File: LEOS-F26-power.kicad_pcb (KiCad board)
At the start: 2 copper layers, 100 x 100 mm, 18 parts, among them J1 MicroFit_1x4, J2 MicroFit_1x4, U1 MCP2518FD, U2 MCP2562FD, Y1 40 MHz

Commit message: updates to BOM
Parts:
- added C-1: 4.7uF, Capacitor_SMD:C_0805_2012Metric, F.Cu at (128.0, 94.4)
- added C-10: 0.1u, Capacitor_SMD:C_0805_2012Metric, F.Cu at (128.0, 115.5)
- added C-2: 4.7uF, Capacitor_SMD:C_0805_2012Metric, F.Cu at (128.0, 97.4)
- added C-3: 4.7uF, Capacitor_SMD:C_0805_2012Metric, F.Cu at (128.0, 100.5)
- added C-4: 4.7uF, Capacitor_SMD:C_0805_2012Metric, F.Cu at (128.0, 103.5)
- added C-5: 0.1u, Capacitor_SMD:C_0805_2012Metric, F.Cu at (128.0, 106.5)
- added C-6: 620p, Capacitor_SMD:C_0805_2012Metric, F.Cu at (128.0, 109.5)
- added C-7: 6.8p, Capacitor_SMD:C_0805_2012Metric, F.Cu at (128.0, 112.5)
- added C-8: 47u, LEOS:CAPAE660X600N, F.Cu at (133.2, 115.0)
- added C-9: 47u, Capacitor_SMD:C_1206_3216Metric, F.Cu at (133.2, 118.4)
- added C_1: 4.7uF, Capacitor_SMD:C_0805_2012Metric, F.Cu at (158.1, 121.0)
- added C_2: 4.7uF, Capacitor_SMD:C_0805_2012Metric, F.Cu at (158.1, 124.0)
- added C_3: 4.7uF, Capacitor_SMD:C_0805_2012Metric, F.Cu at (158.1, 127.0)
- added C_4: 4.7uF, Capacitor_SMD:C_0805_2012Metric, F.Cu at (158.1, 130.0)
- added C_5: 0.1u, Capacitor_SMD:C_0805_2012Metric, F.Cu at (158.1, 133.1)
- added C_6: 4.7n, Capacitor_SMD:C_0805_2012Metric, F.Cu at (158.1, 136.1)
- added C_7: 6.8p, Capacitor_SMD:C_0805_2012Metric, F.Cu at (158.1, 139.1)
- added C_8: 47u, LEOS:CAPAE660X600N, F.Cu at (167.6, 136.4)
- added C_9: 47u, Capacitor_SMD:C_1206_3216Metric, F.Cu at (167.6, 139.8)
- added CdVdt1: 4.7n, Capacitor_SMD:C_0805_2012Metric, F.Cu at (176.5, 94.0)
- added Cin1: 0.1u, Capacitor_SMD:C_0805_2012Metric, F.Cu at (178.0, 104.1)
- added Cin2: 10uF, Capacitor_SMD:C_0805_2012Metric, F.Cu at (180.5, 104.0)
- added Cout1: 10uF, Capacitor_SMD:C_0805_2012Metric, F.Cu at (166.5, 103.5)
- added Cout2: 10uF, Capacitor_SMD:C_0805_2012Metric, F.Cu at (164.0, 103.5)
- added D-1: 60V 20A, Diode_THT:D_DO-201AD_P15.24mm_Horizontal, F.Cu at (133.9, 122.5)
- added D_1: 60V 20A, Diode_THT:D_DO-201AD_P15.24mm_Horizontal, F.Cu at (172.6, 136.2)
- added J3: Power Input, Connector_AMASS:AMASS_XT60IPW-M_1x03_P7.20mm_Horizontal, F.Cu at (183.0, 88.2)
- added J4: 5V, Connector_JST:JST_XH_S2B-XH-A_1x02_P2.50mm_Horizontal, F.Cu at (190.1, 111.2)
- added J5: 5V, Connector_JST:JST_XH_S2B-XH-A_1x02_P2.50mm_Horizontal, F.Cu at (190.0, 120.0)
- added J6: 5V, Connector_JST:JST_XH_S2B-XH-A_1x02_P2.50mm_Horizontal, F.Cu at (190.1, 128.8)
- added J7: 1-18V, Connector_JST:JST_XH_S2B-XH-A_1x02_P2.50mm_Horizontal, F.Cu at (109.9, 108.2)
- added J8: 1-18V, Connector_JST:JST_XH_S2B-XH-A_1x02_P2.50mm_Horizontal, F.Cu at (109.9, 117.2)
- added J9: 1-18V, Connector_JST:JST_XH_S2B-XH-A_1x02_P2.50mm_Horizontal, F.Cu at (109.9, 126.2)
- added L-1: 10uH, LEOS:IND_BOURNS_SRR1280, F.Cu at (138.3, 107.5)
- added L_1: 4.7uH, LEOS:IND_SRP7028A-4R7M_BRN, F.Cu at (170.3, 123.8)
- added R-1: 365k, Resistor_SMD:R_0805_2012Metric, F.Cu at (132.4, 94.4)
- added R-2: 88.7, Resistor_SMD:R_0805_2012Metric, F.Cu at (132.4, 97.3)
- added R-3: 390k, Resistor_SMD:R_0805_2012Metric, F.Cu at (132.4, 100.3)
- added R-4: 56.2k, Resistor_SMD:R_0805_2012Metric, F.Cu at (132.4, 103.2)
- added R-5: 1.1k, Resistor_SMD:R_0805_2012Metric, F.Cu at (132.4, 106.2)
- added R-6: 25.5k, Resistor_SMD:R_0805_2012Metric, F.Cu at (132.4, 109.2)
- added R.1: 150k, Resistor_THT:R_Axial_DIN0207_L6.3mm_D2.5mm_P10.16mm_Horizontal, F.Cu at (150.9, 82.5)
- added R.2: 10k, Resistor_THT:R_Axial_DIN0207_L6.3mm_D2.5mm_P10.16mm_Horizontal, F.Cu at (150.9, 86.5)
- added R_1: 365k, Resistor_SMD:R_0805_2012Metric, F.Cu at (162.5, 121.0)
- added R_2: 88.7, Resistor_SMD:R_0805_2012Metric, F.Cu at (162.5, 123.9)
- added R_3: 147k, Resistor_SMD:R_0805_2012Metric, F.Cu at (162.5, 126.9)
- added R_4: 23.7k, Resistor_SMD:R_0805_2012Metric, F.Cu at (162.5, 129.8)
- added R_5: 60.4k, Resistor_SMD:R_0805_2012Metric, F.Cu at (162.5, 132.8)
- added R_6: 11.5k, Resistor_SMD:R_0805_2012Metric, F.Cu at (162.5, 135.7)
- added R_ILIM1: 3.0k, Resistor_SMD:R_0805_2012Metric, F.Cu at (166.5, 96.0)
- added TP1-18: TestPoint, TestPoint:TestPoint_Loop_D2.60mm_Drill0.9mm_Beaded, F.Cu at (109.5, 101.5)
- added TPFB1-18: TestPoint, TestPoint:TestPoint_Loop_D2.60mm_Drill0.9mm_Beaded, F.Cu at (158.9, 98.2)
- added TPFB5: TestPoint, TestPoint:TestPoint_Loop_D2.60mm_Drill0.9mm_Beaded, F.Cu at (151.9, 98.2)
- added TPGND2: GND TestPoint, TestPoint:TestPoint_Loop_D2.60mm_Drill0.9mm_Beaded, F.Cu at (103.5, 101.0)
- added TPUVLO1: TestPoint, TestPoint:TestPoint_Loop_D2.60mm_Drill0.9mm_Beaded, F.Cu at (151.9, 91.1)
- added U3: TPS54540BDDA, LEOS:SO-POWERPAD8_DDA_TEX, F.Cu at (169.0, 131.4)
- added U4: TPS16630PWPR, LEOS:HTSSOP20_PWP_TEX, F.Cu at (172.0, 100.1)
- added U5: TPS54540BDDA, LEOS:SO-POWERPAD8_DDA_TEX, F.Cu at (122.7, 125.6)
- added U6: MCP41HV51-104E/MQ, LEOS:QFN20_5x5MC_MCH, F.Cu at (139.8, 93.9)
- renumbered TP3 to TP5V1, TP4 to TPGND1
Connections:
- A1 pad 14: unconnected-(A1-GPIO10-Pad14) -> /SCK1
- A1 pad 15: unconnected-(A1-GPIO11-Pad15)_1 -> /MOSI1
- A1 pad 16: unconnected-(A1-GPIO12-Pad16) -> /MISO1
- A1 pad 17: unconnected-(A1-GPIO13-Pad17) -> /CS1
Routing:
- added copper zone on F.Cu, net +BATT
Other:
- board text removed: "Be sure to update the information block at the bottom of the page! (Then delete me)"

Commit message: efuse routing
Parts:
- moved R.1 24.0 mm to (172.0, 94.0), turned to 180 degrees
- moved Cin2 12.6 mm to (174.5, 93.0), turned to 90 degrees
- moved R.2 11.8 mm to (161.8, 91.0)
- moved Cin1 11.1 mm to (177.0, 93.0), turned to 90 degrees
- moved Cout2 10.8 mm to (174.5, 106.0)
- moved Cout1 10.3 mm to (176.5, 106.0)
- moved CdVdt1 10.3 mm to (167.0, 98.0), turned to -90 degrees
- moved R_ILIM1 6.47 mm to (167.0, 102.4)
- turned U4 to -90 degrees
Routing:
- net Net-(U4-UVLO): track 0.00 -> 14.0 mm
- net +BATT: track 0.00 -> 3.49 mm
- net Net-(U4-ILIM): track 0.00 -> 2.22 mm
- net Net-(U4-DVDT): track 0.00 -> 2.19 mm
- net GND: vias 22 -> 42
- added copper zone on In1.Cu, net GND
- added copper zone on F.Cu, net VPP
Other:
- copper layers 2 -> 4

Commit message: efuse routing 2
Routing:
- net GND: track 4.46 -> 15.2 mm, vias 42 -> 40
- net +BATT: track 3.49 -> 6.02 mm
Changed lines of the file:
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@@
+	)
+	(segment
+		(start 169.772299 97.172313)
+		(end 170.422285 97.172313)
+		(width 0.25)
+		(layer "F.Cu")
+		(net "GND")
+	)
+	(segment
+		(start 169.772299 98.772299)
+		(end 170 99)
+		(width 0.25)
+		(layer "F.Cu")
+		(net "GND")
+	)
+	(segment
+		(start 167 98.9)
+		(end 168.9 98.9)
+		(width 1)
+		(layer "F.Cu")
+		(net "GND")
 	)
 	(segment
@@
 	)
 	(segment
+		(start 174.5 106.95)
+		(end 176.5 106.95)
+		(width 0.5)
+		(layer "F.Cu")
+		(net "GND")
+	)
+	(segment
+		(start 167 98.9)
+		(end 167 101.5)
+		(width 1)
+		(layer "F.Cu")
+		(net "GND")
+	)
+	(segment
+		(start 168.9 98.9)
+		(end 169 99)
+		(width 1)
+		(layer "F.Cu")
+		(net "GND")
+	)
+	(segment
 		(start 124.512501 73.512501)
 		(end 124.45 73.575001)
@@
 	)
 	(segment
+		(start 169.772299 97.172313)
+		(end 169.772299 98.772299)
+		(width 0.25)
+		(layer "F.Cu")
+		(net "GND")
+	)
+	(segment
+		(start 176.5 106.95)
+		(end 177.95 106.95)
+		(width 0.5)
+		(layer "F.Cu")
+		(net "GND")
+	)
+	(segment
+		(start 177.95 106.95)
+		(end 178 107)
+		(width 0.5)
+		(layer "F.Cu")
+		(net "GND")
+	)
+	(segment
 		(start 125.025001 73)
 		(end 124.512501 73.512501)
@@
 	)
 	(via
-		(at 179 107)
-		(size 0.6)
-		(drill 0.3)
-		(layers "F.Cu" "B.Cu")
-		(free yes)
-		(net "GND")
-	)
-	(via
 		(at 136.25 78)
 		(size 0.6)
@@
 		)
 		(filling no)
-		(net "GND")
-	)
-	(via
-		(at 168 100)
-		(size 0.6)
-		(drill 0.3)
-		(layers "F.Cu" "B.Cu")
-		(free yes)
 		(net "GND")
 	)
@@
 	)
 	(segment
+		(start 174.45 94)
+		(end 174.5 93.95)
+		(width 1)
+		(layer "F.Cu")
+		(net "+BATT")
+	)
+	(segment
 		(start 171.722257 97.172313)
 		(end 171.722257 96.277743)
@@
 		(end 174 95.5)
 		(width 0.2)
+		(layer "F.Cu")
+		(net "+BATT")
+	)
+	(segment
+		(start 172 94)
+		(end 174.45 94)
+		(width 1)
 		(layer "F.Cu")
 		(net "+BATT")
@@
 	)
 	(zone
-		(net "GND")
-		(layer "F.Cu")
-		(name "GND_5")
-		(hatch edge 0.5)
-		(priority 12)
-		(connect_pads
-			(clearance 0.25)
-		)
-		(min_thickness 0.25)
-		(fill
-			(thermal_gap 0.3)
-			(thermal_bridge_width 0.5)
-			(island_removal_mode 0)
-		)
-		(polygon
-			(pts
-				(xy 173.5 106) (xy 180 106) (xy 180 108) (xy 173.5 108)
-			)
-		)
-	)
-	(zone
 		(net "+BATT")
 		(layer "F.Cu")
@@
 		(polygon
 			(pts
-				(xy 170 89) (xy 178 89) (xy 178 93) (xy 170 93)
+				(xy 170 89) (xy 179 89) (xy 179 93) (xy 170 93)
 			)
 		)
@@
 				(xy 131.116421 72.282843) (xy 131.257842 72.141422) (xy 130.931066 71.743934) (xy 130.675706 71.700707)
 				(xy 130.846465 72.29573)
-			)
-		)
-	)
-	(zone
-		(net "+BATT")
-		(layer "F.Cu")
-		(name "BATT_2")
-		(hatch edge 0.5)
-		(priority 5)
-		(connect_pads
-			(clearance 0.25)
-		)
-		(min_thickness 0.25)
-		(fill yes
-			(thermal_gap 0.3)
-			(thermal_bridge_width 0.5)
-			(island_removal_mode 0)
-		)
-		(polygon
-			(pts
-				(xy 173.5 93) (xy 171 93) (xy 171 95) (xy 173.5 95)
 			)
 		)
@@
 		(polygon
 			(pts
-				(xy 166 98) (xy 174 98) (xy 174 102) (xy 166 102)
+				(xy 168 98) (xy 174 98) (xy 174 102) (xy 168 102)
 			)
 		)
@@
 		(net "GND")
 		(layer "F.Cu")
-		(name "GND_2")
 		(hatch edge 0.5)
-		(priority 9)
+		(priority 2)
+		(connect_pads
+			(clearance 0.25)
+		)
+		(min_thickness 0.25)
+		(fill yes
+			(thermal_gap 0.25)
+			(thermal_bridge_width 0.5)
+			(island_removal_mode 0)
+		)
+		(polygon
+			(pts
+				(xy 109 74.5) (xy 109 78) (xy 113.5 78) (xy 113.5 74.5)
+			)
+		)
+	)
+	(zone
+		(net "+BATT")
+		(layer "F.Cu")
+		(name "BATT_1")
+		(hatch edge 0.5)
+		(priority 4)
 		(connect_pads
 			(clearance 0.25)
@@
 		(polygon
 			(pts
-				(xy 169.5 96.3) (xy 170.7 96.3) (xy 170.7 98.1) (xy 169.5 98.1)
+				(xy 173.5 98) (xy 173.5 93) (xy 178.5 93) (xy 178.5 98)
 			)
 		)
-	)
-	(zone
-		(net "GND")
-		(layer "F.Cu")
-		(hatch edge 0.5)
-		(priority 2)
-		(connect_pads
-			(clearance 0.25)
-		)
-		(min_thickness 0.25)
-		(fill yes
-			(thermal_gap 0.25)
-			(thermal_bridge_width 0.5)
-			(island_removal_mode 0)
-		)
-		(polygon
-			(pts
-				(xy 109 74.5) (xy 109 78) (xy 113.5 78) (xy 113.5 74.5)
-			)
-		)
-	)
-	(zone
-		(net "+BATT")
-		(layer "F.Cu")
-		(name "BATT_1")
-		(hatch edge 0.5)
-		(priority 4)
-		(connect_pads
-			(clearance 0.25)
-		)
-		(min_thickness 0.25)
-		(fill yes
-			(thermal_gap 0.3)
-			(thermal_bridge_width 0.5)
-			(island_removal_mode 0)
-		)
-		(polygon
-			(pts
-				(xy 173.5 98) (xy 173.5 93) (xy 175.5 93) (xy 175.5 98)
-			)
-		)

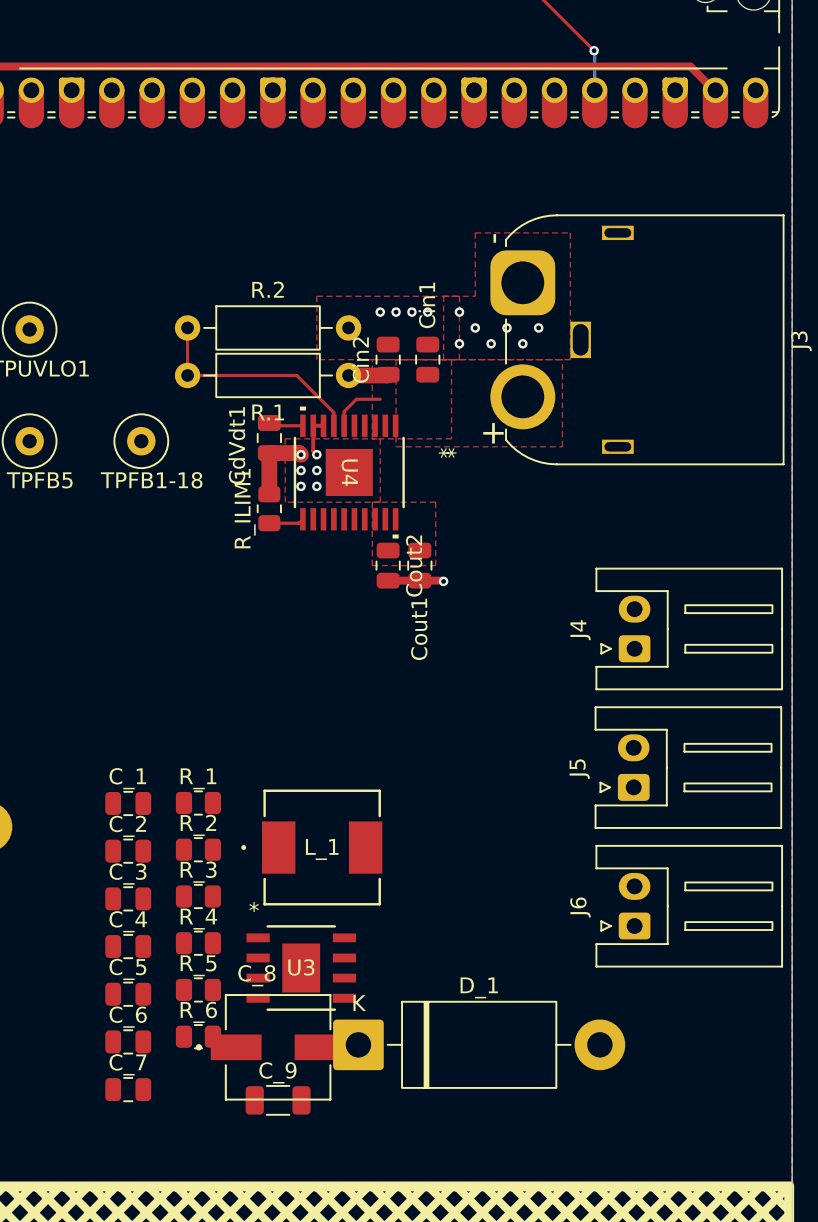
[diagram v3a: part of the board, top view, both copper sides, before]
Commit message: buck converter routing
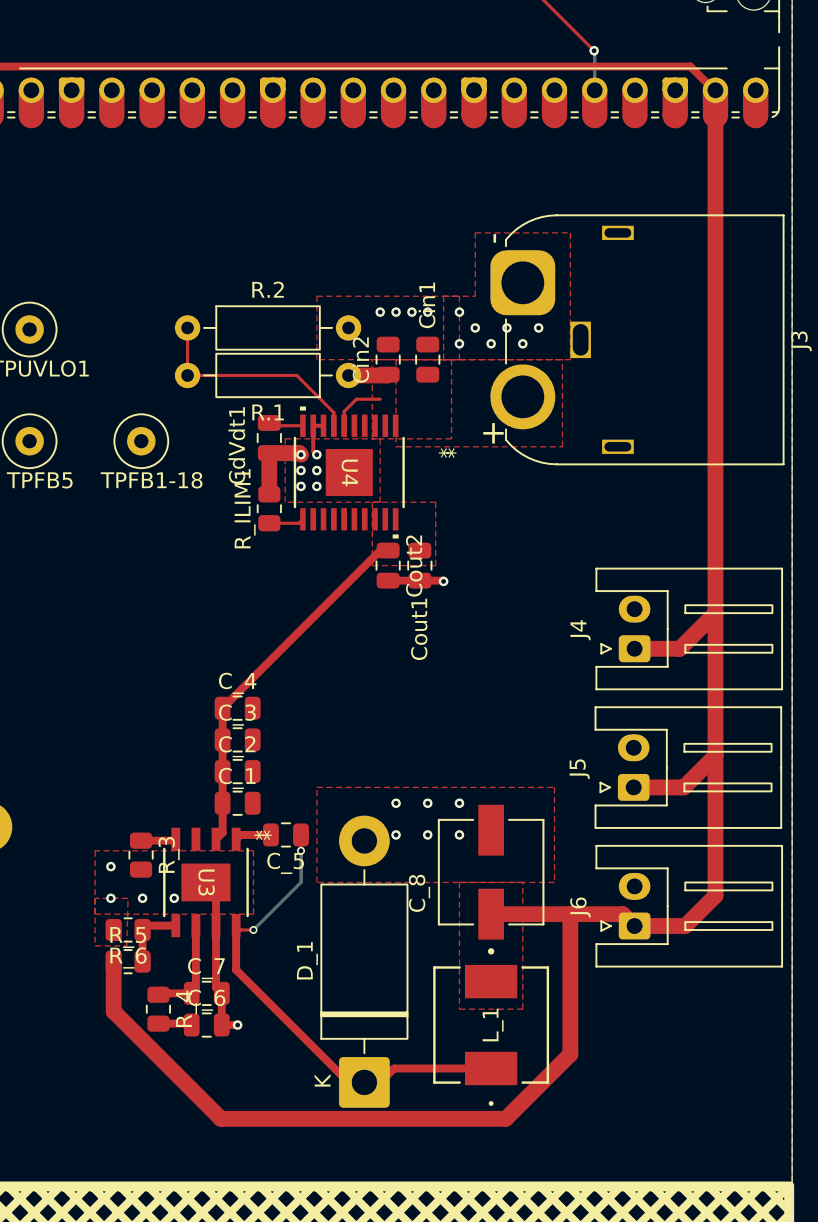
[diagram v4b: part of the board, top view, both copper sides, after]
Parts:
- removed C_9: 47u, Capacitor_SMD:C_1206_3216Metric
- removed R_1: 365k, Resistor_SMD:R_0805_2012Metric
- removed R_2: 88.7, Resistor_SMD:R_0805_2012Metric
- moved C_8 17.4 mm to (181.0, 125.3), turned to 90 degrees
- moved C_4 16.6 mm to (165.0, 115.0)
- moved L_1 15.5 mm to (181.0, 135.0), turned to 90 degrees
- moved C_5 14.1 mm to (168.1, 123.0), turned to 180 degrees
- moved C_3 12.2 mm to (165.0, 117.0)
- moved C_2 8.54 mm to (165.0, 119.0)
- moved U3 8.08 mm to (163.0, 126.0), turned to -90 degrees
- moved R_6 8.07 mm to (158.1, 129.0), turned to 180 degrees
- moved C_7 7.84 mm to (163.1, 133.0)
- moved C_1 6.91 mm to (165.0, 121.0)
- moved C_6 5.07 mm to (163.1, 135.0)
- moved R_4 4.87 mm to (160.0, 134.0), turned to -90 degrees
- moved R_5 4.78 mm to (158.1, 131.0)
- moved R_3 4.46 mm to (158.9, 124.3), turned to -90 degrees
- moved D_1 2.40 mm to (173.0, 138.6), turned to 90 degrees
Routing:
- net +5V: track 104.0 -> 226.7 mm
- net Net-(D_1-K): track 0.00 -> 29.7 mm, vias 0 -> 2
- net VPP: track 0.00 -> 23.0 mm
- net GND: track 15.2 -> 25.6 mm, vias 40 -> 51
- net Net-(U3-COMP): track 0.00 -> 6.52 mm
- net /5V Power/FB: track 0.00 -> 4.21 mm
- net Net-(U3-BOOT): track 0.00 -> 2.31 mm
- net Net-(U3-RT/CLK): track 0.00 -> 2.23 mm
- net Net-(C_6-Pad1): track 0.00 -> 2.14 mm

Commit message: routing done
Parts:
- removed C-9: 47u, Capacitor_SMD:C_1206_3216Metric
- removed R-1: 365k, Resistor_SMD:R_0805_2012Metric
- removed R-2: 88.7, Resistor_SMD:R_0805_2012Metric
- moved C-10 25.2 mm to (126.5, 90.3)
- moved C-8 21.1 mm to (126.5, 135.0), turned to -90 degrees
- moved L-1 19.5 mm to (126.0, 122.6), turned to -90 degrees
- moved U5 19.3 mm to (127.5, 106.8), turned to 180 degrees
- moved D-1 15.9 mm to (119.4, 116.0)
- moved C-1 14.2 mm to (134.0, 107.3), turned to -90 degrees
- moved R-4 13.5 mm to (119.0, 104.8), turned to 180 degrees
- moved C-2 12.7 mm to (136.0, 107.3), turned to -90 degrees
- moved C-4 12.6 mm to (140.0, 107.3), turned to -90 degrees
- moved C-3 12.1 mm to (138.0, 107.3), turned to -90 degrees
- moved R-6 11.2 mm to (123.5, 102.3)
- moved R-5 10.7 mm to (123.5, 100.3), turned to 180 degrees
- moved C-6 10.1 mm to (118.0, 107.8), turned to -90 degrees
- moved C-7 9.22 mm to (120.0, 107.9), turned to -90 degrees
- moved U6 7.01 mm to (132.8, 94.3), turned to 180 degrees
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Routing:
- net VPP: track 23.0 -> 28.8 mm
- net Net-(U5-COMP): track 0.00 -> 2.14 mm
- net Net-(C-6-Pad1): track 0.00 -> 2.09 mm
- net /1-18V Power/FB1: track 0.00 -> 2.00 mm
- net Net-(D_1-K): vias 2 -> 0

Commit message: updates to BOM
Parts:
- moved TPFB5 37.5 mm to (152.1, 135.6)
- moved TPFB1-18 33.1 mm to (125.9, 95.3)
- moved TPGND2 16.3 mm to (118.9, 95.7)
- moved C-9 13.2 mm to (139.5, 88.0)
- moved TPUVLO1 11.6 mm to (162.0, 85.5)
- moved C-8 10.5 mm to (134.5, 128.2), turned to 90 degrees
- moved U6 5.96 mm to (138.6, 92.8)
- moved R-1 5.07 mm to (129.0, 102.5), turned to 180 degrees
- moved TP1-18 4.61 mm to (105.0, 100.5)
- moved L-1 4.61 mm to (123.0, 126.1)
- moved R-3 2.00 mm to (124.5, 102.1), turned to 90 degrees
- moved C-7 1.44 mm to (120.5, 106.5)
- moved C-6 1.44 mm to (118.5, 106.5)
- moved R-2 1.44 mm to (119.5, 103.5)
- moved C-1 1.30 mm to (134.5, 108.5)
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- renumbered C-10 to C-9, R-3 to R-1, R-4 to R-2, R-5 to R-3, R-6 to R-4, R_3 to R_1, R_4 to R_2, R_5 to R_3, R_6 to R_4
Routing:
- net VDC: track 0.00 -> 89.4 mm
- net GND: track 25.6 -> 78.1 mm, vias 51 -> 72
- net VDD: track 90.8 -> 141.7 mm, vias 3 -> 7
- net /CS1: track 0.00 -> 48.9 mm, vias 0 -> 2
- net /SCK1: track 0.00 -> 48.8 mm, vias 0 -> 2
- net /MOSI1: track 0.00 -> 47.7 mm, vias 0 -> 2
- net /MISO1: track 0.00 -> 44.9 mm, vias 0 -> 2
- net VPP: track 28.8 -> 63.0 mm
- net Net-(D-1-K): track 0.00 -> 25.3 mm
- net /1-18V Power/POT: track 0.00 -> 15.8 mm
- net /1-18V Power/FB1: track 2.00 -> 12.9 mm, vias 0 -> 2
- net /5V Power/FB: track 4.21 -> 13.7 mm, vias 0 -> 2
- net Net-(U4-UVLO): track 14.0 -> 19.6 mm
- net Net-(U5-COMP): track 2.14 -> 6.67 mm
- net Net-(U5-BOOT): track 0.00 -> 2.81 mm
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- added copper zone on F.Cu, net VDC
